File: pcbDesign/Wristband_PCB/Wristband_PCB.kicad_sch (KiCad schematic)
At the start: 5 parts, among them U1 module_adxl345, U2 SEN0344, U3 ESP32-C3_SUPERMINI_TH

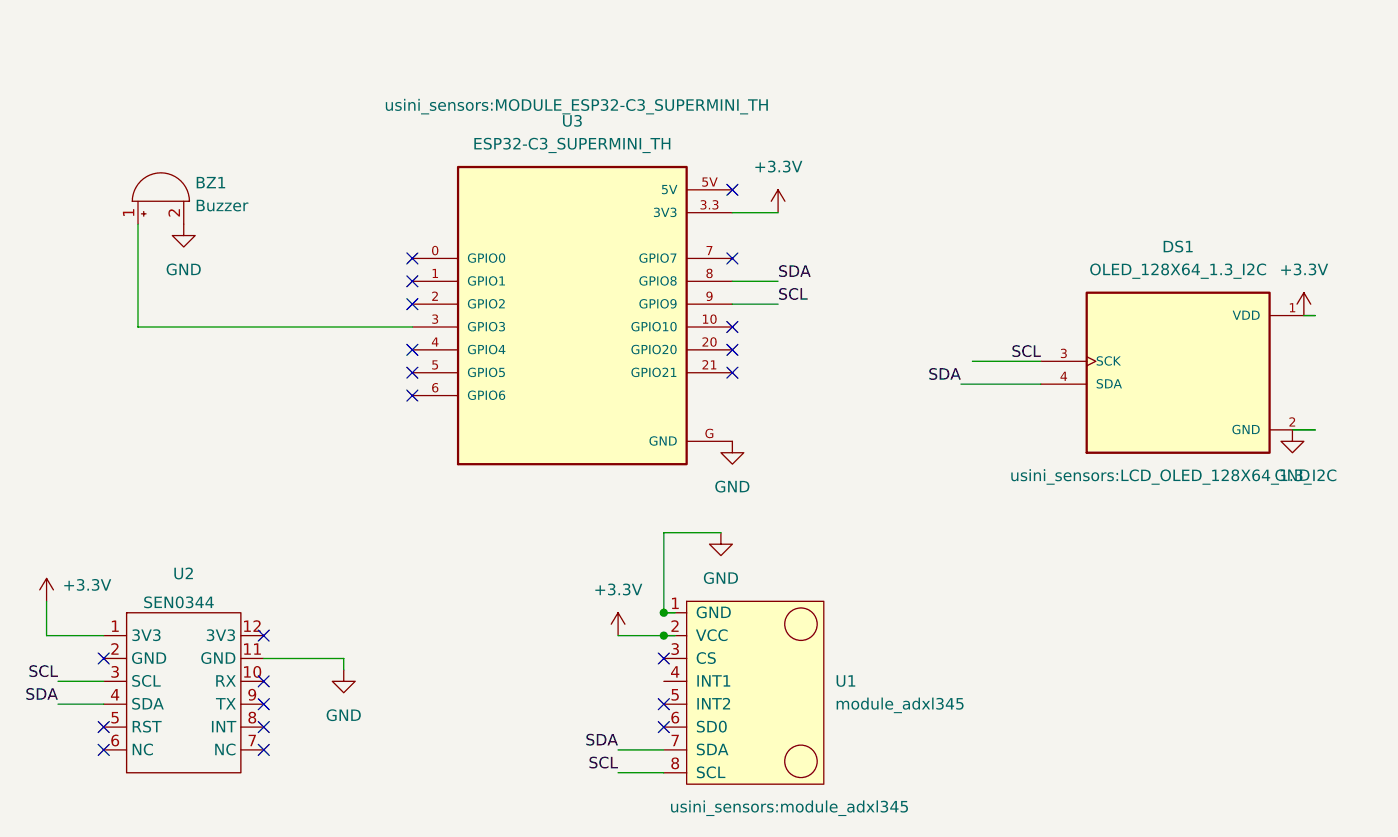
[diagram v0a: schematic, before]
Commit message: added the power terminal and the resistor
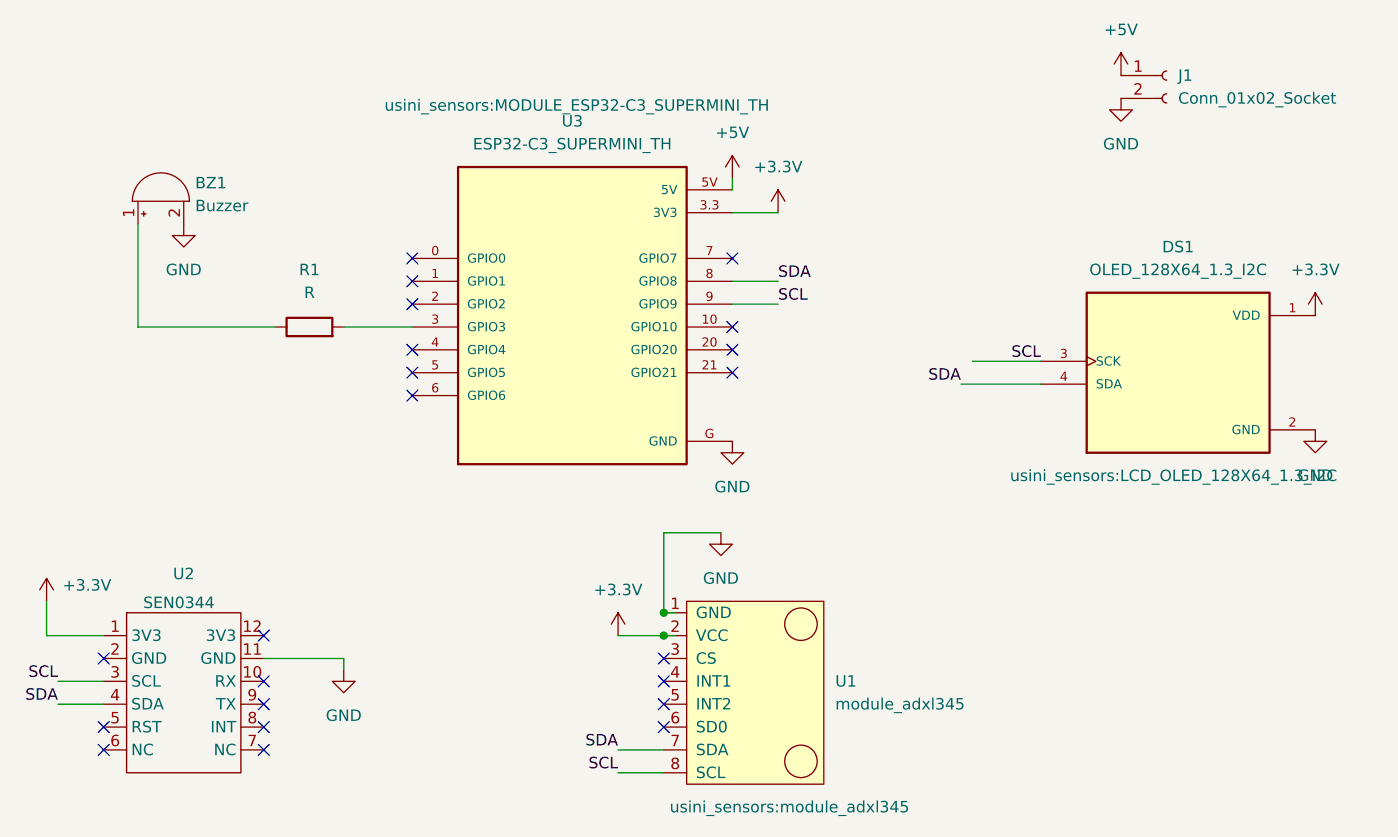
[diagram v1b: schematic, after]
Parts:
- added J1: Conn_01x02_Socket, Connector_PinSocket_2.54mm:PinSocket_1x02_P2.54mm_Vertical, symbol Connector:Conn_01x02_Socket
- added R1: R, Resistor_THT:R_Axial_DIN0204_L3.6mm_D1.6mm_P5.08mm_Horizontal, symbol Device:R
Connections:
- net GND: now also J1.2 (Pin_2)
- net at U3.3 (GPIO3): now also R1.2; no longer BZ1.1 (+)
- net +5V: now reaches U3.5V
- net +5V: now also J1.1 (Pin_1)
- new net: BZ1.1 (+), R1.1
